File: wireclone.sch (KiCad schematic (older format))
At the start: 33 parts, among them U1 LME49720, U2 LME49720, U3 LME49600, U4 LME49600

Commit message: checked in all subsheets
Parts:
- removed C1, C2, C3, C4, C5, C6: 1u, Capacitors_SMD:C_1206, symbol C
- removed C10, C11, C14, C15: 100n, Capacitors_SMD:C_0805, symbol C
- removed C12, C13, C16, C9: 10u, Capacitors_Tantalum_SMD:Tantalum_Case-C_EIA-6032-28_Reflow, symbol CP
- removed C7, C8: 1u, Capacitors_SMD:C_0805, symbol C
- removed R1, R10, R3, R7, R8, R9: 1k, Resistors_SMD:R_0805, symbol R
- removed R2, R4, R5, R6: 1M, Resistors_SMD:R_0805, symbol R
- removed R? (x2): 0R, Resistors_SMD:R_0805, symbol R
- removed RV1: 10k, symbol DUAL_POT
- removed U1, U2: LME49720, SMD_Packages:SOIC-8-N, symbol LME49720
- removed U3, U4: LME49600, symbol LME49600
- added P2, P3: CONN_01X03, Terminal_Blocks:TerminalBlock_Pheonix_MKDS1.5-3pol, symbol CONN_01X03
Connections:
- net labels removed: OUTL, OUTR, VCC, VEE
- wire segments 93 -> 16

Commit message: did most of the layout
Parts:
- P2, P3: footprint Terminal_Blocks:TerminalBlock_Pheonix_MKDS1.5-3pol -> Terminal_Blocks:TerminalBlock_Pheonix_MPT-2.54mm_3pol
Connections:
- wire segments 16 -> 13
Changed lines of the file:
@@
 $Descr A4 11693 8268
 encoding utf-8
-Sheet 1 4
+Sheet 1 3
 Title ""
 Date ""
@@
 F 0 "P2" H 6200 2300 50  0000 C CNN
 F 1 "CONN_01X03" V 6300 2100 50  0000 C CNN
-F 2 "Terminal_Blocks:TerminalBlock_Pheonix_MKDS1.5-3pol" H 6200 2100 50  0001 C CNN
+F 2 "Terminal_Blocks:TerminalBlock_Pheonix_MPT-2.54mm_3pol" H 6200 2100 50  0001 C CNN
 F 3 "" H 6200 2100 50  0000 C CNN
 	1    6200 2100
@@
 F 0 "P3" H 9250 2300 50  0000 C CNN
 F 1 "CONN_01X03" V 9350 2100 50  0000 C CNN
-F 2 "Terminal_Blocks:TerminalBlock_Pheonix_MKDS1.5-3pol" H 9250 2100 50  0001 C CNN
+F 2 "Terminal_Blocks:TerminalBlock_Pheonix_MPT-2.54mm_3pol" H 9250 2100 50  0001 C CNN
 F 3 "" H 9250 2100 50  0000 C CNN
 	1    9250 2100
@@
 Text Label 6450 2100 0    60   ~ 0
 GND
-$Sheet
-S 3000 1900 900  1000
-U 584AFB40
-F0 "xformer" 60
-F1 "xformer.sch" 60
-F2 "AC1" O R 3900 2300 60
-F3 "AC2" O R 3900 2400 60
-F4 "GND" O R 3900 2700 60
-$EndSheet
-Wire Wire Line
-	3900 2700 4200 2700
-Wire Wire Line
-	3900 2400 4400 2400
-Wire Wire Line
-	3900 2300 4400 2300
-Text Label 4000 2700 0    60   ~ 0
-GND
 $EndSCHEMATC

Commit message: moved output to end, stitched thermal plane
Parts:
- P2, P3: footprint Terminal_Blocks:TerminalBlock_Pheonix_MPT-2.54mm_3pol -> Pin_Headers:Pin_Header_Straight_1x03_Pitch2.54mm
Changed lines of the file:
@@
 F 0 "P2" H 6200 2300 50  0000 C CNN
 F 1 "CONN_01X03" V 6300 2100 50  0000 C CNN
-F 2 "Terminal_Blocks:TerminalBlock_Pheonix_MPT-2.54mm_3pol" H 6200 2100 50  0001 C CNN
+F 2 "Pin_Headers:Pin_Header_Straight_1x03_Pitch2.54mm" H 6200 2100 50  0001 C CNN
 F 3 "" H 6200 2100 50  0000 C CNN
 	1    6200 2100
@@
 F 0 "P3" H 9250 2300 50  0000 C CNN
 F 1 "CONN_01X03" V 9350 2100 50  0000 C CNN
-F 2 "Terminal_Blocks:TerminalBlock_Pheonix_MPT-2.54mm_3pol" H 9250 2100 50  0001 C CNN
+F 2 "Pin_Headers:Pin_Header_Straight_1x03_Pitch2.54mm" H 9250 2100 50  0001 C CNN
 F 3 "" H 9250 2100 50  0000 C CNN
 	1    9250 2100

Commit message: complete layout drafted
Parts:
- removed P2: CONN_01X03, Pin_Headers:Pin_Header_Straight_1x03_Pitch2.54mm, symbol CONN_01X03
- added P2, P4: CONN_01X02, Pin_Headers:Pin_Header_Straight_1x02_Pitch2.54mm, symbol CONN_01X02
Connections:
- wire segments 13 -> 15
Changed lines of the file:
@@
 F6 "AC2" I L 4400 2400 60
 $EndSheet
-$Comp
-L CONN_01X03 P2
-U 1 1 584AA0FA
-P 6200 2100
-F 0 "P2" H 6200 2300 50  0000 C CNN
-F 1 "CONN_01X03" V 6300 2100 50  0000 C CNN
-F 2 "Pin_Headers:Pin_Header_Straight_1x03_Pitch2.54mm" H 6200 2100 50  0001 C CNN
-F 3 "" H 6200 2100 50  0000 C CNN
-	1    6200 2100
-	-1   0    0    1
-$EndComp
 Wire Wire Line
-	6400 2100 6600 2100
-Wire Wire Line
-	6400 2000 6850 2000
-Wire Wire Line
-	6850 2000 6850 2100
+	6850 1800 6850 2100
 $Comp
 L CONN_01X03 P3
@@
 GND
 Wire Wire Line
-	6400 2200 7000 2200
+	6150 2200 7000 2200
 Wire Wire Line
 	6850 2100 7000 2100
@@
 Wire Wire Line
 	5500 2700 7000 2700
-Text Label 6250 2600 0    60   ~ 0
+Text Label 6350 2600 0    60   ~ 0
 GND
-Text Label 6450 2100 0    60   ~ 0
-GND
+$Comp
+L CONN_01X02 P2
+U 1 1 59F1B351
+P 5950 1850
+F 0 "P2" H 5950 2000 50  0000 C CNN
+F 1 "CONN_01X02" V 6050 1850 50  0000 C CNN
+F 2 "Pin_Headers:Pin_Header_Straight_1x02_Pitch2.54mm" H 5950 1850 50  0001 C CNN
+F 3 "" H 5950 1850 50  0000 C CNN
+	1    5950 1850
+	-1   0    0    -1
+$EndComp
+$Comp
+L CONN_01X02 P4
+U 1 1 59F1B7BD
+P 5950 2250
+F 0 "P4" H 5950 2400 50  0000 C CNN
+F 1 "CONN_01X02" V 6050 2250 50  0000 C CNN
+F 2 "Pin_Headers:Pin_Header_Straight_1x02_Pitch2.54mm" H 5950 2250 50  0001 C CNN
+F 3 "" H 5950 2250 50  0000 C CNN
+	1    5950 2250
+	-1   0    0    -1
+$EndComp
+Wire Wire Line
+	6850 1800 6150 1800
+Wire Wire Line
+	6150 2600 6150 2300
+Connection ~ 6150 2600
+Wire Wire Line
+	6150 1900 6250 1900
+Wire Wire Line
+	6250 1900 6250 2600
+Connection ~ 6250 2600
 $EndSCHEMATC

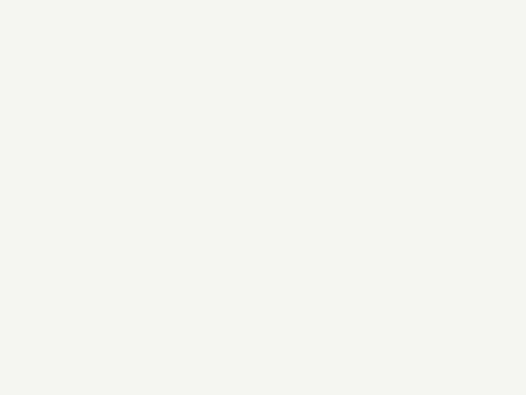
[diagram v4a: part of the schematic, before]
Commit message: added fiducials
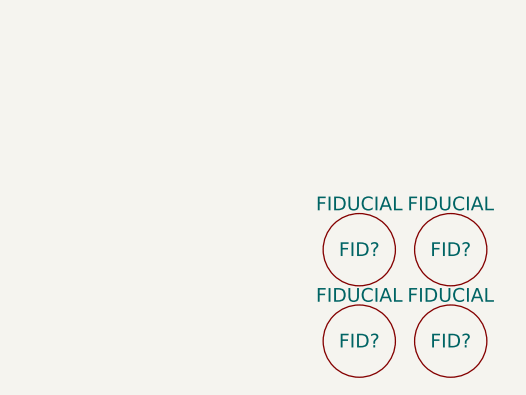
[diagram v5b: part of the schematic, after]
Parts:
- added FID? (x4): FIDUCIAL, smd:FID0.5, symbol FIDUCIAL
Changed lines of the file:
@@
 	6250 1900 6250 2600
 Connection ~ 6250 2600
+$Comp
+L FIDUCIAL FID?
+U 1 1 59F1CCBA
+P 8800 5500
+F 0 "FID?" H 8800 5500 60  0000 C CNN
+F 1 "FIDUCIAL" H 8800 5700 60  0000 C CNN
+F 2 "smd:FID0.5" H 8800 5500 60  0001 C CNN
+F 3 "" H 8800 5500 60  0000 C CNN
+	1    8800 5500
+	1    0    0    -1
+$EndComp
+$Comp
+L FIDUCIAL FID?
+U 1 1 59F1D516
+P 9200 5500
+F 0 "FID?" H 9200 5500 60  0000 C CNN
+F 1 "FIDUCIAL" H 9200 5700 60  0000 C CNN
+F 2 "smd:FID0.5" H 9200 5500 60  0001 C CNN
+F 3 "" H 9200 5500 60  0000 C CNN
+	1    9200 5500
+	1    0    0    -1
+$EndComp
+$Comp
+L FIDUCIAL FID?
+U 1 1 59F1D58D
+P 9200 5900
+F 0 "FID?" H 9200 5900 60  0000 C CNN
+F 1 "FIDUCIAL" H 9200 6100 60  0000 C CNN
+F 2 "smd:FID0.5" H 9200 5900 60  0001 C CNN
+F 3 "" H 9200 5900 60  0000 C CNN
+	1    9200 5900
+	1    0    0    -1
+$EndComp
+$Comp
+L FIDUCIAL FID?
+U 1 1 59F1D603
+P 8800 5900
+F 0 "FID?" H 8800 5900 60  0000 C CNN
+F 1 "FIDUCIAL" H 8800 6100 60  0000 C CNN
+F 2 "smd:FID0.5" H 8800 5900 60  0001 C CNN
+F 3 "" H 8800 5900 60  0000 C CNN
+	1    8800 5900
+	1    0    0    -1
+$EndComp
 $EndSCHEMATC

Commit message: cleanup, rev.a as manufactured
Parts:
- gave numbers to parts that had none: 4
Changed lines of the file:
@@
 Connection ~ 6250 2600
 $Comp
-L FIDUCIAL FID?
+L FIDUCIAL FID1
 U 1 1 59F1CCBA
 P 8800 5500
-F 0 "FID?" H 8800 5500 60  0000 C CNN
+F 0 "FID1" H 8800 5500 60  0000 C CNN
 F 1 "FIDUCIAL" H 8800 5700 60  0000 C CNN
 F 2 "smd:FID0.5" H 8800 5500 60  0001 C CNN
@@
 $EndComp
 $Comp
-L FIDUCIAL FID?
+L FIDUCIAL FID2
 U 1 1 59F1D516
 P 9200 5500
-F 0 "FID?" H 9200 5500 60  0000 C CNN
+F 0 "FID2" H 9200 5500 60  0000 C CNN
 F 1 "FIDUCIAL" H 9200 5700 60  0000 C CNN
 F 2 "smd:FID0.5" H 9200 5500 60  0001 C CNN
@@
 $EndComp
 $Comp
-L FIDUCIAL FID?
+L FIDUCIAL FID4
 U 1 1 59F1D58D
 P 9200 5900
-F 0 "FID?" H 9200 5900 60  0000 C CNN
+F 0 "FID4" H 9200 5900 60  0000 C CNN
 F 1 "FIDUCIAL" H 9200 6100 60  0000 C CNN
 F 2 "smd:FID0.5" H 9200 5900 60  0001 C CNN
@@
 $EndComp
 $Comp
-L FIDUCIAL FID?
+L FIDUCIAL FID3
 U 1 1 59F1D603
 P 8800 5900
-F 0 "FID?" H 8800 5900 60  0000 C CNN
+F 0 "FID3" H 8800 5900 60  0000 C CNN
 F 1 "FIDUCIAL" H 8800 6100 60  0000 C CNN
 F 2 "smd:FID0.5" H 8800 5900 60  0001 C CNN
